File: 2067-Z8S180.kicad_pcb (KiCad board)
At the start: 4 copper layers, 59 x 78 mm, 9 parts, among them J1 Conn_02x12_Odd_Even, J2 Conn_02x30_Odd_Even, U1 Z8S18020FSG, U2 IS61WV20488BLL-10TLI

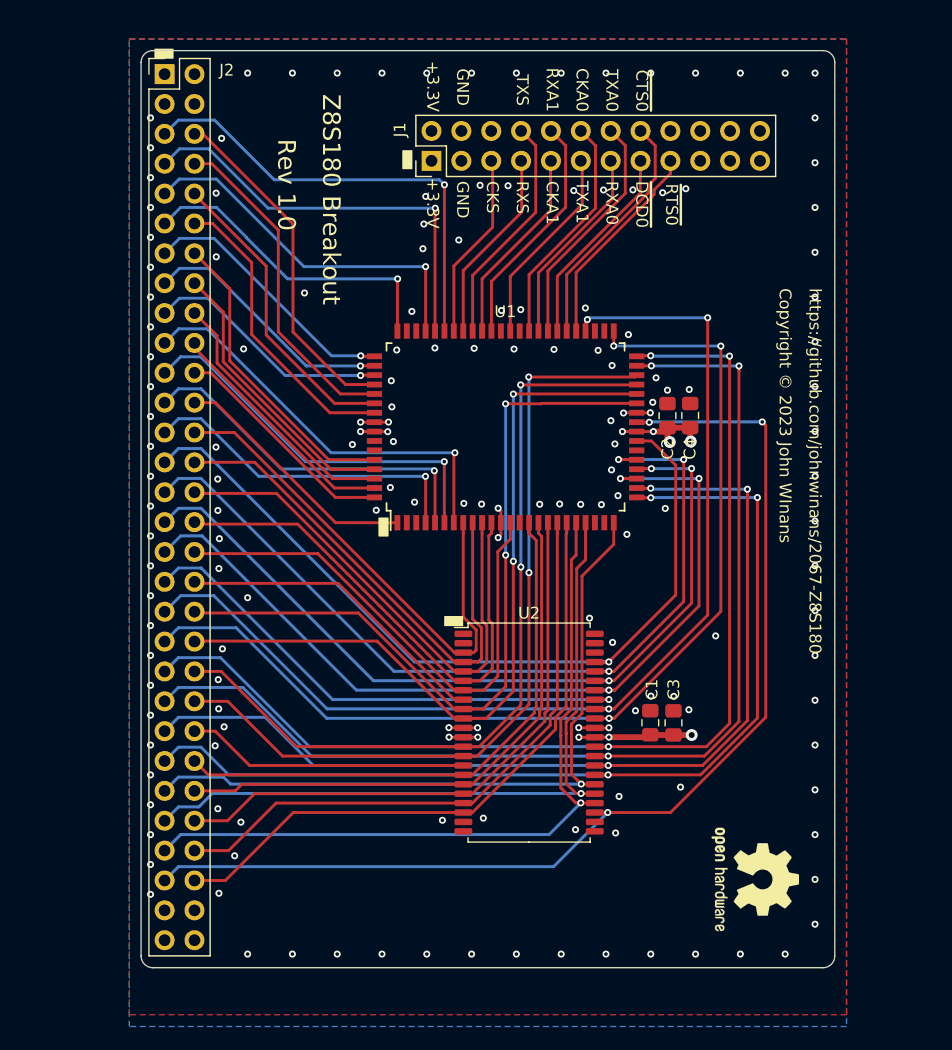
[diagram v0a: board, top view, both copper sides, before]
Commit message: Fix CPU footprint, M1/DREQ, and mounting holes
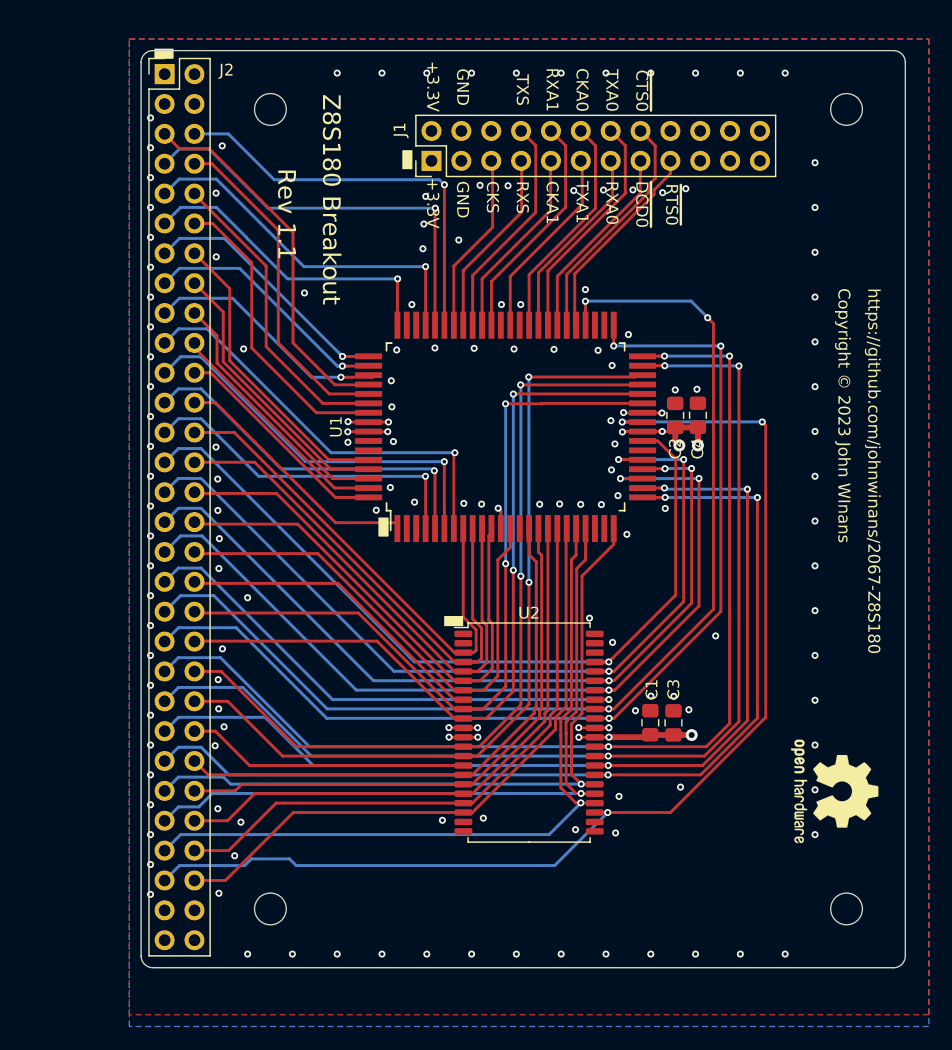
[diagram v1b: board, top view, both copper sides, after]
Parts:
- added H1: MountingHole, MountingHole:MountingHole_2.7mm_M2.5, F.Cu at (101.0, 45.0)
- added H2: MountingHole, MountingHole:MountingHole_2.7mm_M2.5, F.Cu at (150.0, 45.0)
- added H3: MountingHole, MountingHole:MountingHole_2.7mm_M2.5, F.Cu at (101.0, 113.0)
- added H4: MountingHole, MountingHole:MountingHole_2.7mm_M2.5, F.Cu at (150.0, 113.0)
- U1: footprint Package_QFP:PQFP-80_14x20mm_P0.8mm -> jb-footprint:PQFP-80_14x20mm_P0.8mm
- U2: value IS61WV20488BLL-10TLI -> IS61WV10248EDBLL-10TLI
- moved LOGO1 10.1 mm to (149.0, 103.0)
- moved C4 0.66 mm to (137.4, 71.0)
- moved C2 0.66 mm to (135.4, 71.0)
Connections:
- J2 pad 5: /~DREQ1 -> /~M1
- J2 pad 6: /~M1 -> /~DREQ1
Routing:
- net /~DREQ1: track 39.0 -> 35.5 mm
- net /D7: track 91.9 -> 95.2 mm
- net /A19: track 93.9 -> 96.8 mm
- net GND: track 14.7 -> 17.5 mm, vias 164 -> 155
- net /~M1: track 29.5 -> 32.2 mm
- net +3V3: track 21.1 -> 22.4 mm
- net /PHI: track 25.6 -> 26.2 mm
- net /~RD: track 26.2 -> 26.8 mm
- net /~WR: track 28.5 -> 29.0 mm
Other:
- board size 59 x 78 mm -> 65 x 78 mm
- board text added: "Rev 1.1"
- board text removed: "Rev 1.0"

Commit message: Widen board & add J2 labels
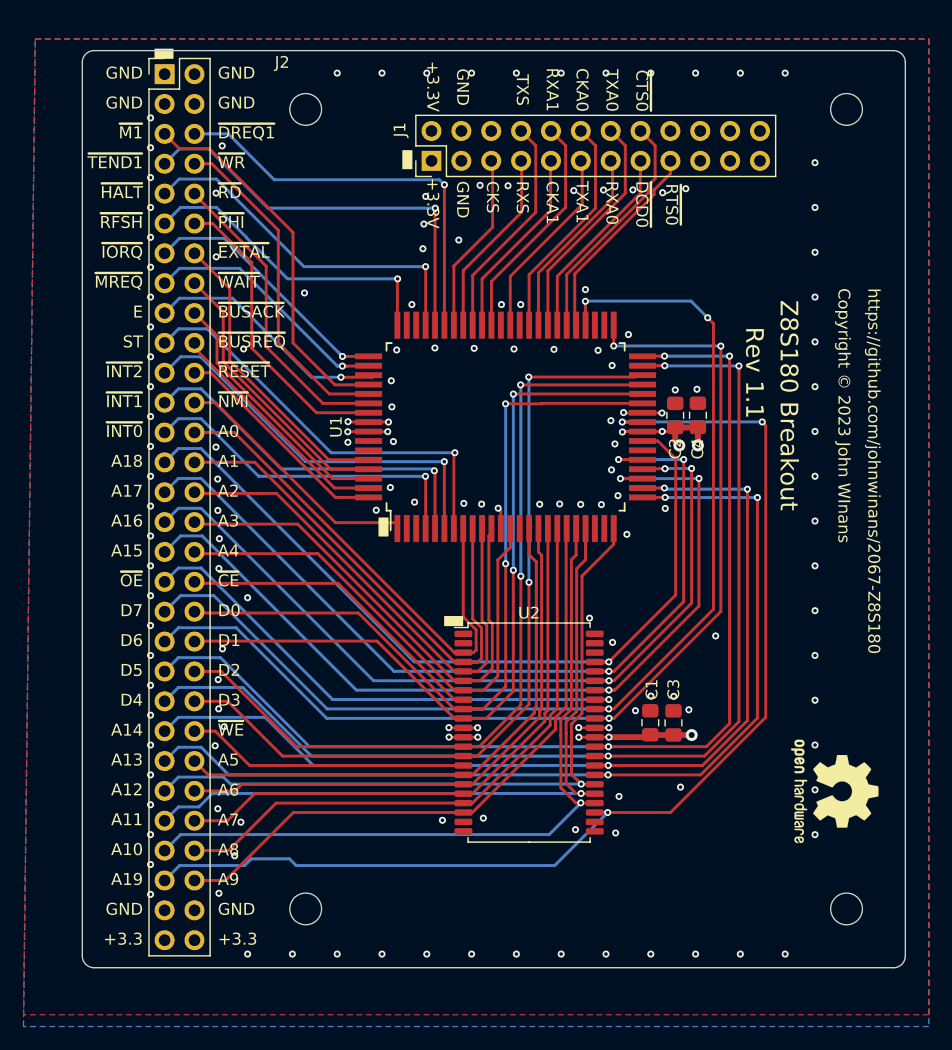
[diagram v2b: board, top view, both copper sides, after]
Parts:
- moved H1 3.00 mm to (104.0, 45.0)
- moved H3 3.00 mm to (104.0, 113.0)
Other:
- board size 65 x 78 mm -> 70 x 78 mm
- board text added: "+3.3"
- board text added: "A0"
- board text added: "A1"
- board text added: "A10"
- board text added: "A11"
- board text added: "A12"
- board text added: "A13"
- board text added: "A14"
- board text added: "A15"
- board text added: "A16"
- board text added: "A17"
- board text added: "A18"
- board text added: "A19"
- board text added: "A2"
- board text added: "A3"
- board text added: "A4"
- board text added: "A5"
- board text added: "A6"
- board text added: "A7"
- board text added: "A8"
- board text added: "A9"
- board text added: "D0"
- board text added: "D1"
- board text added: "D2"
- board text added: "D3"
- board text added: "D4"
- board text added: "D5"
- board text added: "D6"
- board text added: "D7"
- board text added: "E"
- board text added: "ST"
- board text added: "~BUSACK"
- board text added: "~BUSREQ"
- board text added: "~CE"
- board text added: "~DREQ1"
- board text added: "~EXTAL"
- board text added: "~HALT"
- board text added: "~INT0"
- board text added: "~INT1"
- board text added: "~INT2"
- board text added: "~IORQ"
- board text added: "~M1"
- board text added: "~MREQ"
- board text added: "~NMI"
- board text added: "~OE"
- board text added: "~PHI"
- board text added: "~RD"
- board text added: "~RESET"
- board text added: "~RFSH"
- board text added: "~TEND1"
- board text added: "~WAIT"
- board text added: "~WE"
- board text added: "~WR"

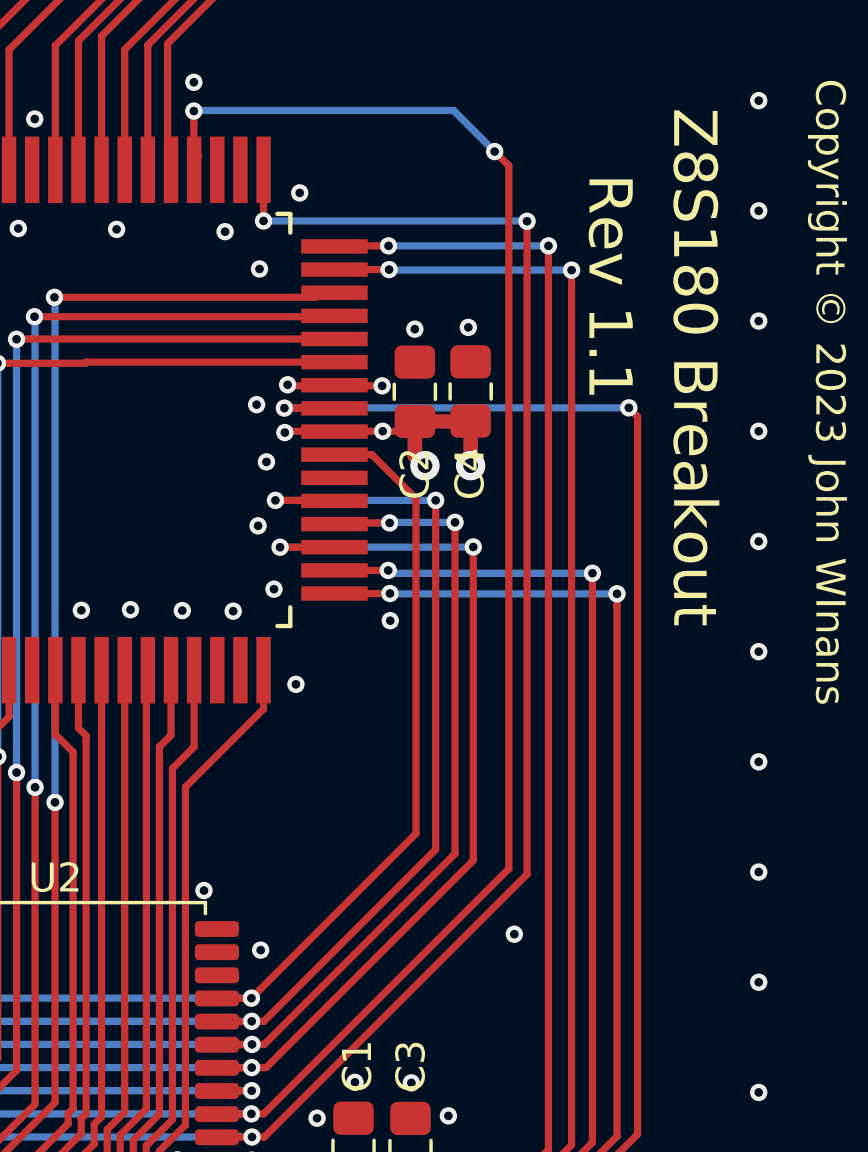
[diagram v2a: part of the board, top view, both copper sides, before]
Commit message: Thermal relief, SRAM A20
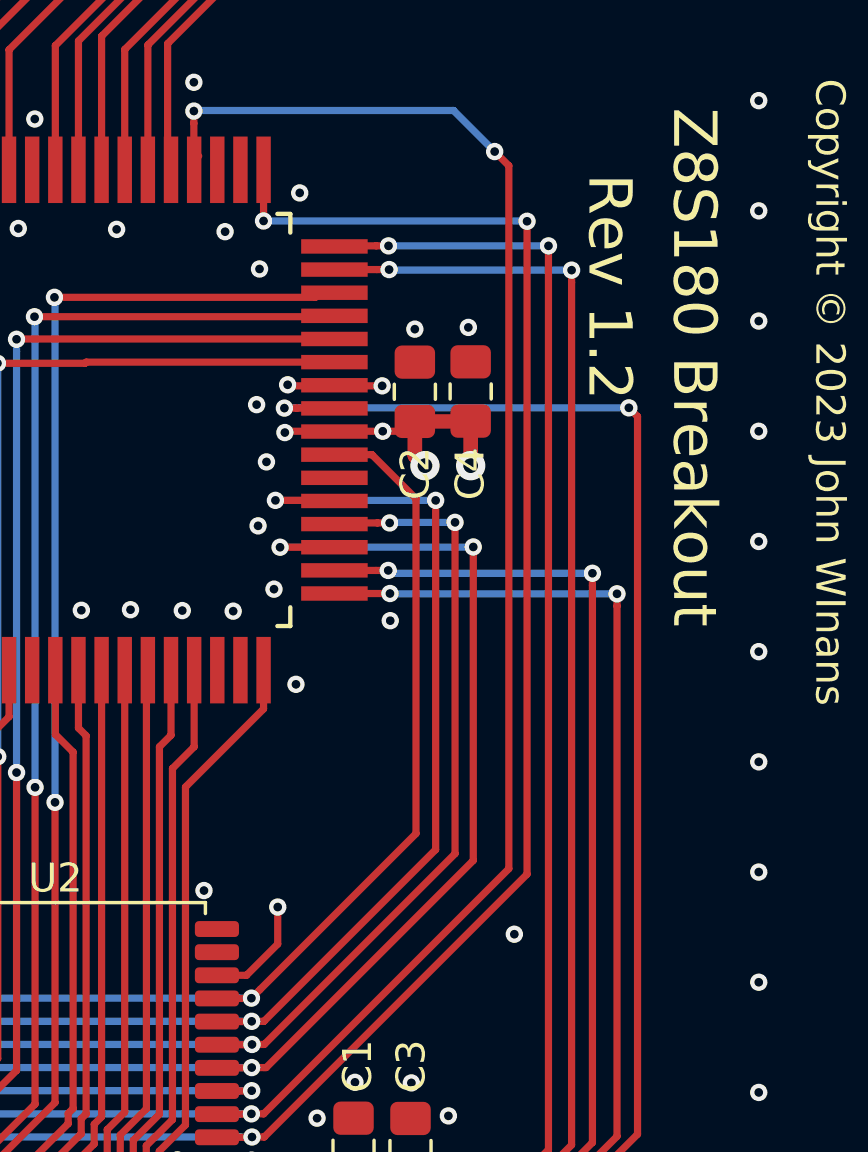
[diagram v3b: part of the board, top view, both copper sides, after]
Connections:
- U2 pad 42: Net-(U2-Pad42) -> GND
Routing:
- net GND: track 17.5 -> 21.4 mm
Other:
- board text added: "Rev 1.2"
- board text removed: "Rev 1.1"
